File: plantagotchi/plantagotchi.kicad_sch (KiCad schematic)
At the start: 2 parts, among them J1 Conn_01x04_Socket, U1 102010428

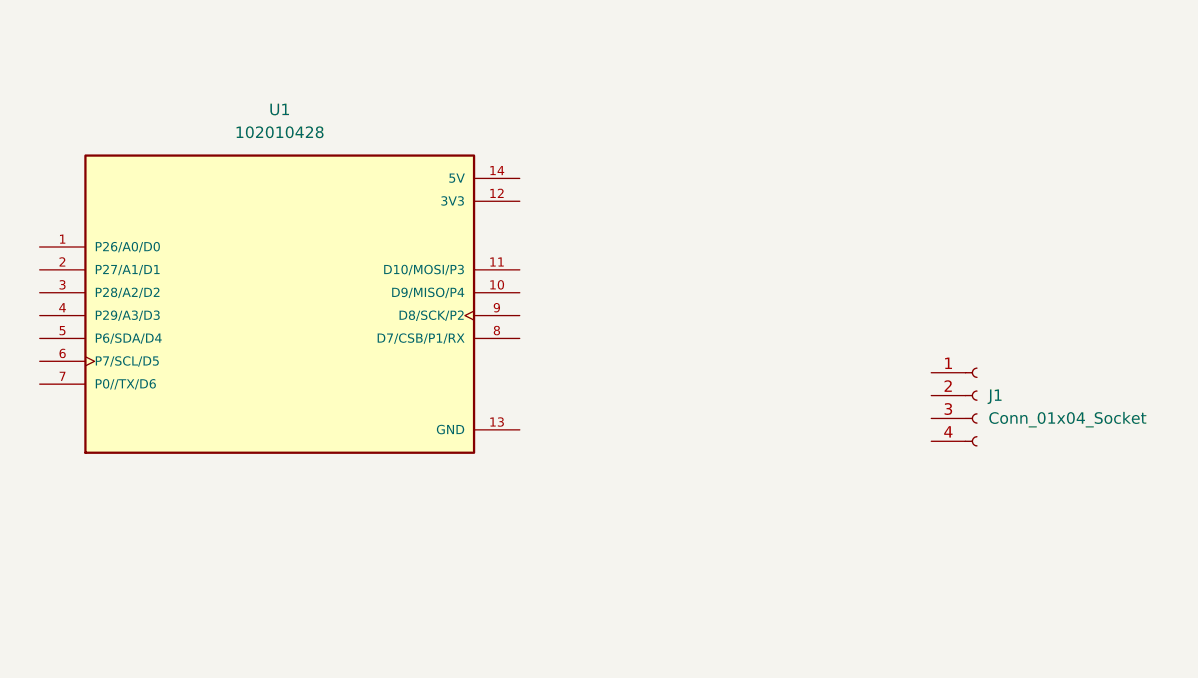
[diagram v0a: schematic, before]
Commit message: wiring diagram
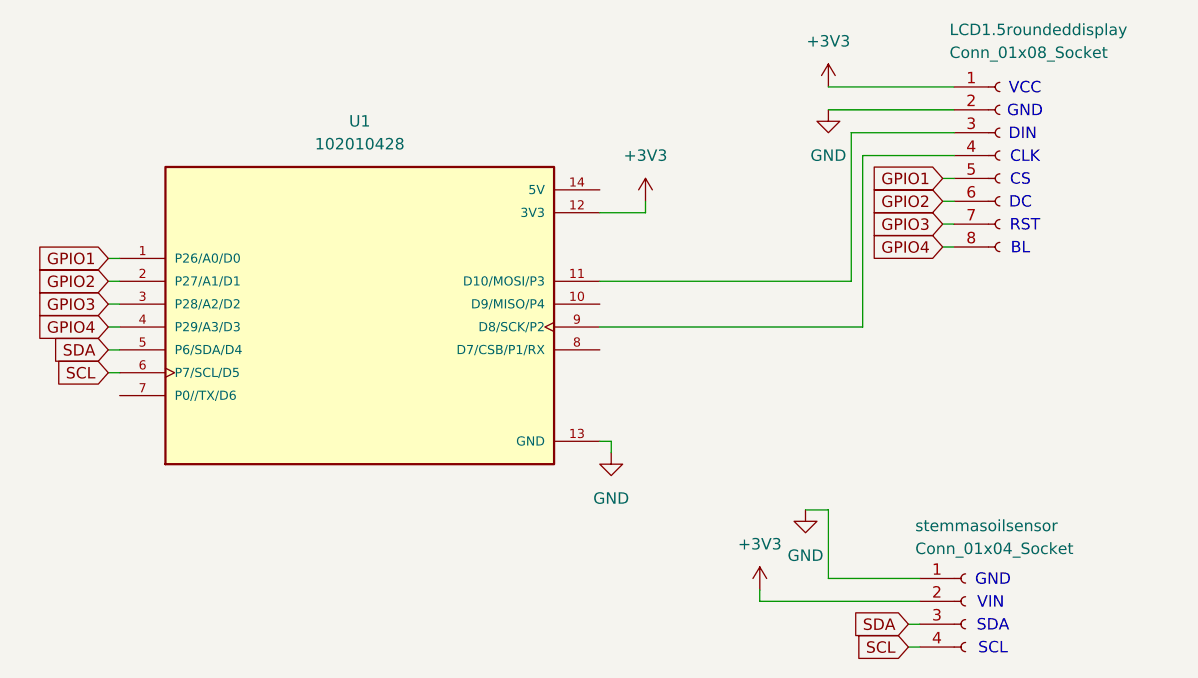
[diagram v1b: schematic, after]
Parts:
- added LCD1.5roundeddisplay: Conn_01x08_Socket, symbol Connector:Conn_01x08_Socket
- renumbered J1 to stemmasoilsensor
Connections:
- net GND: now reaches stemmasoilsensor.1 (Pin_1)
- net GND: now also U1.13 (GND), LCD1.5roundeddisplay.2 (Pin_2)
- net +3V3: now reaches stemmasoilsensor.2 (Pin_2)
- net +3V3: now also U1.12 (3V3), LCD1.5roundeddisplay.1 (Pin_1)
- net SDA: now reaches stemmasoilsensor.3 (Pin_3)
- net SDA: now also U1.5 (P6/SDA/D4)
- net SCL: now reaches stemmasoilsensor.4 (Pin_4)
- net SCL: now also U1.6 (P7/SCL/D5)
- net GPIO1: now reaches U1.1 (P26/A0/D0)
- net GPIO1: now also LCD1.5roundeddisplay.5 (Pin_5)
- net at U1.11 (D10/MOSI/P3): now also LCD1.5roundeddisplay.3 (Pin_3)
- net GPIO2: now reaches U1.2 (P27/A1/D1)
- net GPIO2: now also LCD1.5roundeddisplay.6 (Pin_6)
- net GPIO3: now reaches U1.3 (P28/A2/D2)
- net GPIO3: now also LCD1.5roundeddisplay.7 (Pin_7)
- net GPIO4: now reaches U1.4 (P29/A3/D3)
- net GPIO4: now also LCD1.5roundeddisplay.8 (Pin_8)
- net at U1.9 (D8/SCK/P2): now also LCD1.5roundeddisplay.4 (Pin_4)
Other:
- note added: "BL"
- note added: "CLK"
- note added: "CS"
- note added: "DC"
- note added: "DIN"
- note added: "GND"
- note added: "RST"
- note added: "SCL"
- note added: "SDA"
- note added: "VCC"
- note added: "VIN"
- moved on the sheet: U1, stemmasoilsensor
